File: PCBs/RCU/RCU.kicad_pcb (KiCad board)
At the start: 4 copper layers, 99 x 139 mm, 148 parts, among them J100 Conn_01x02, J200 USB_C_Receptacle_USB2.0, J201 Conn_01x05, J300 Right_Motor_Screw_Terminal, J301 Right_Encoder_Conn, J302 Left_Motor_Screw_Terminal, J303 Left_Encoder_Conn, J400 USB_C_Receptacle_USB2.0, Q400 2N7002NXAKR (NMOS), Q401 2N7002NXAKR (NMOS), Q402 BSS84AK,215 (PMOS), Q403 2N7002NXAKR (NMOS), SW201 SW_Push, SW400 SW_Push, SW401 SW_SPDT, U100 LM2576S-ADJ, U101 AP63203WU, U102 AZ1117-3.3, U200 STM32G0B1CBT6, U201 USBLC6-2SC6, U300 OPA320, U301 DRV8876, U302 OPA320, U303 DRV8876, U400 USBLC6-2SC6, U401 CH340C, U402 ESP32-MINI-1, U403 DG2788ADN-T1-GE4, U500 APDS-9306-065, U501 LSM6DS3, U502 SHT30-DIS, U600 ADC121C027CIMK/NOPB, U601 OPA320, U602 ADC121C027CIMK/NOPB, U603 OPA320, U700 SST26VF032BT-104I/SM, Y200 16MHz

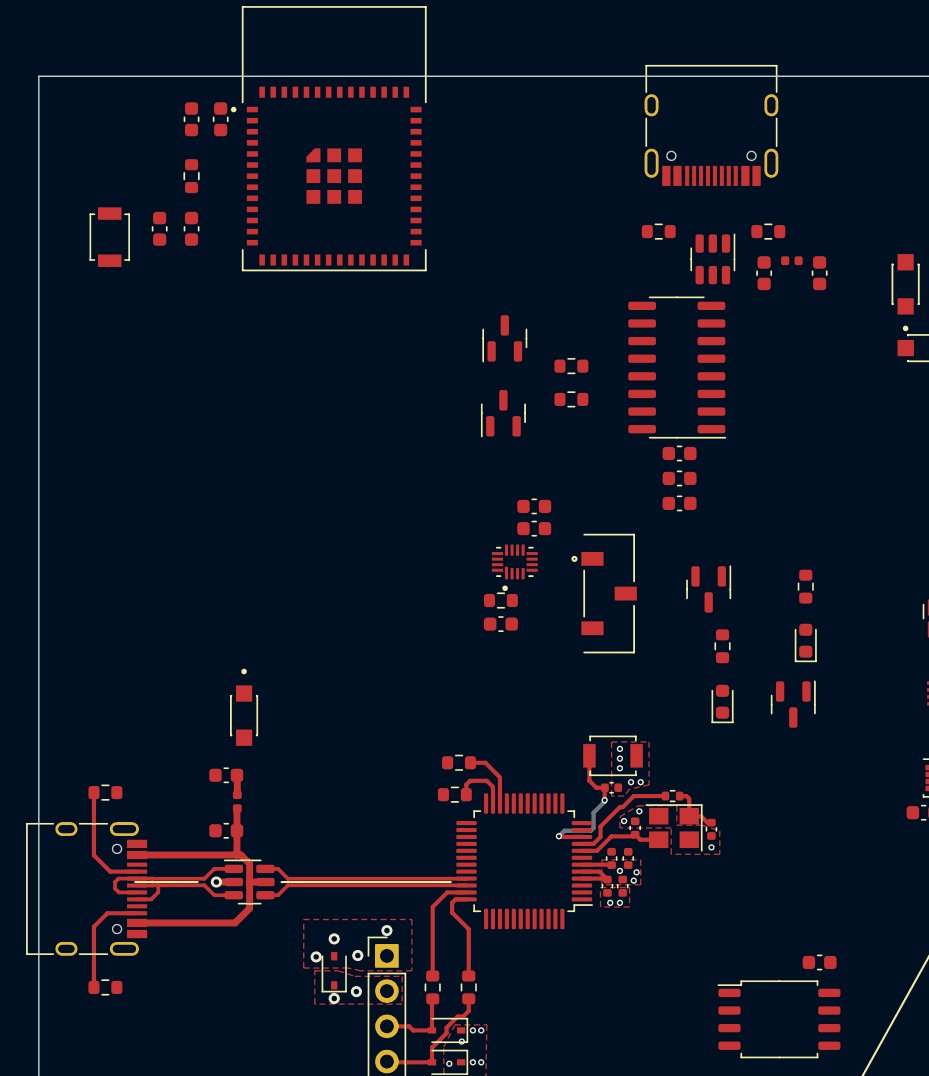
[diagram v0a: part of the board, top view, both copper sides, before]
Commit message: changed pad clearance of uart selector to 0.1mm
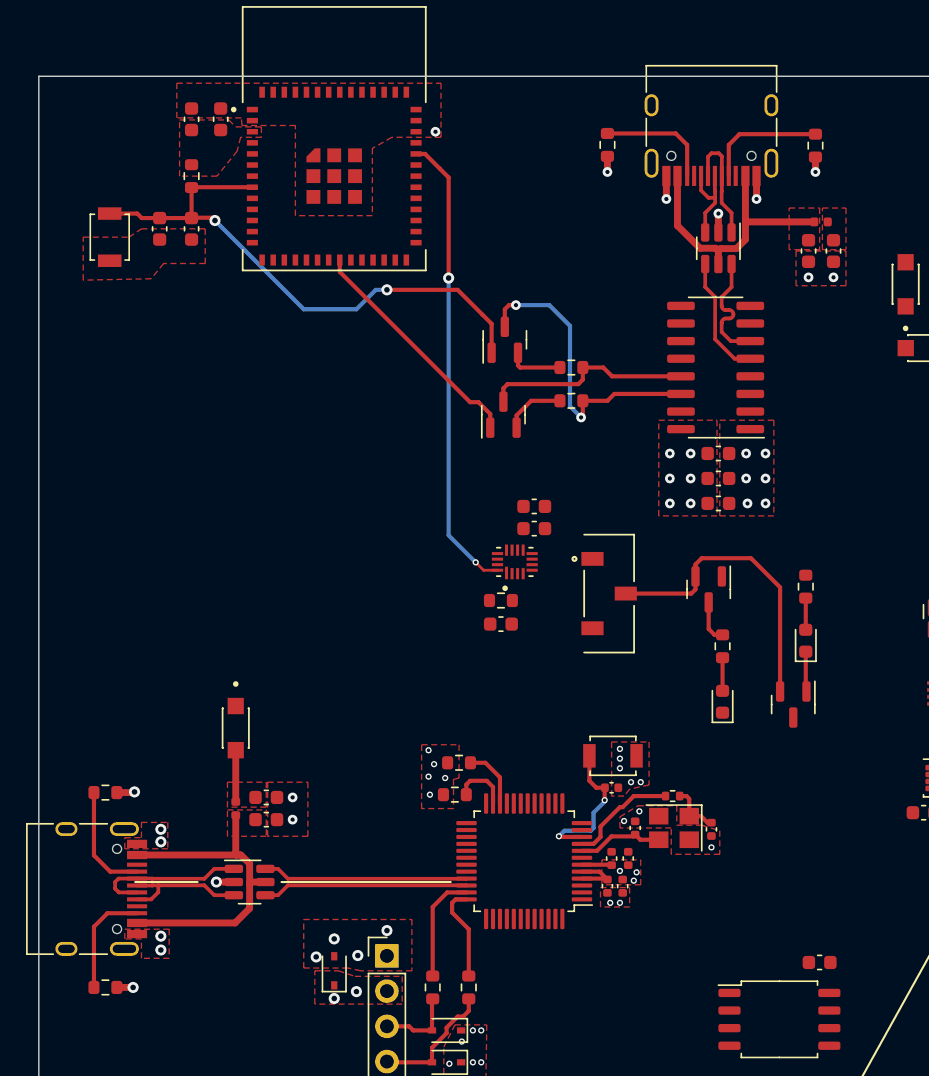
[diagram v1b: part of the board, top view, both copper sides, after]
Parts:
- moved R401 7.26 mm to (109.0, 25.9), turned to 90 degrees
- moved R400 7.07 mm to (124.0, 26.0), turned to -90 degrees
- moved C111 3.58 mm to (123.5, 33.6)
- moved L103 3.50 mm to (124.4, 31.5)
- moved C108 3.30 mm to (84.4, 73.0), turned to 0 degrees
- moved C107 3.00 mm to (84.4, 74.6), turned to 0 degrees
- moved C400 2.80 mm to (117.0, 51.8)
- moved C401 2.80 mm to (117.0, 50.0)
- moved C402 2.80 mm to (117.0, 48.2)
- moved U401 2.80 mm to (116.8, 42.0)
- moved C112 1.89 mm to (125.3, 33.6)
- moved D102 1.08 mm to (82.2, 68.0)
- moved U400 0.89 mm to (117.0, 33.4)
- moved L102 0.51 mm to (82.2, 73.8)
- moved Q400 0.10 mm to (101.5, 45.4)
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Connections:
- C111 pad 1: /[1] Power/VBUS2 -> VBUS2
- J200 pad S1: GND -> unconnected-(J200-PadS1)
- J400 pad A4: /[4] Bluetooth/VBUS2 -> VBUS2
- J400 pad A9: /[4] Bluetooth/VBUS2 -> VBUS2
- J400 pad B4: /[4] Bluetooth/VBUS2 -> VBUS2
- J400 pad B9: /[4] Bluetooth/VBUS2 -> VBUS2
- J400 pad S1: GND -> unconnected-(J400-PadS1)
- L103 pad 1: /[1] Power/VBUS2 -> VBUS2
- U400 pad 5: /[4] Bluetooth/VBUS2 -> VBUS2
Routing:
- net /[4] Bluetooth/BT_EN: track 0.00 -> 40.7 mm, vias 0 -> 2
- net UART_BT_TX: track 0.00 -> 33.4 mm, vias 0 -> 2
- net /[4] Bluetooth/RTS: track 0.00 -> 22.2 mm, vias 0 -> 2
- net /[4] Bluetooth/UART_SELECT: track 0.00 -> 21.6 mm
- net VBUS2: track 0.00 -> 20.1 mm
- net /[4] Bluetooth/IO0: track 0.00 -> 16.9 mm
- net /[4] Bluetooth/DTR: track 0.00 -> 15.2 mm
- net GND: track 1.26 -> 10.6 mm, vias 22 -> 44
- net /[4] Bluetooth/BT_D+: track 0.00 -> 8.84 mm
- net /[4] Bluetooth/CC1: track 0.00 -> 8.81 mm
- net /[4] Bluetooth/BT_D-: track 0.00 -> 8.67 mm
- net /[4] Bluetooth/BT_Raw_D-: track 0.00 -> 8.37 mm
- net /[4] Bluetooth/CC2: track 0.00 -> 8.33 mm
- net /[4] Bluetooth/BT_Raw_D+: track 0.00 -> 6.66 mm
- net /[4] Bluetooth/RTS_R: track 0.00 -> 4.45 mm
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- added copper zone on F.Cu, net +5C
- added copper zone on F.Cu, net +5F
- added copper zone on F.Cu, net VBUS1
- added copper zone on F.Cu, net VBUS2

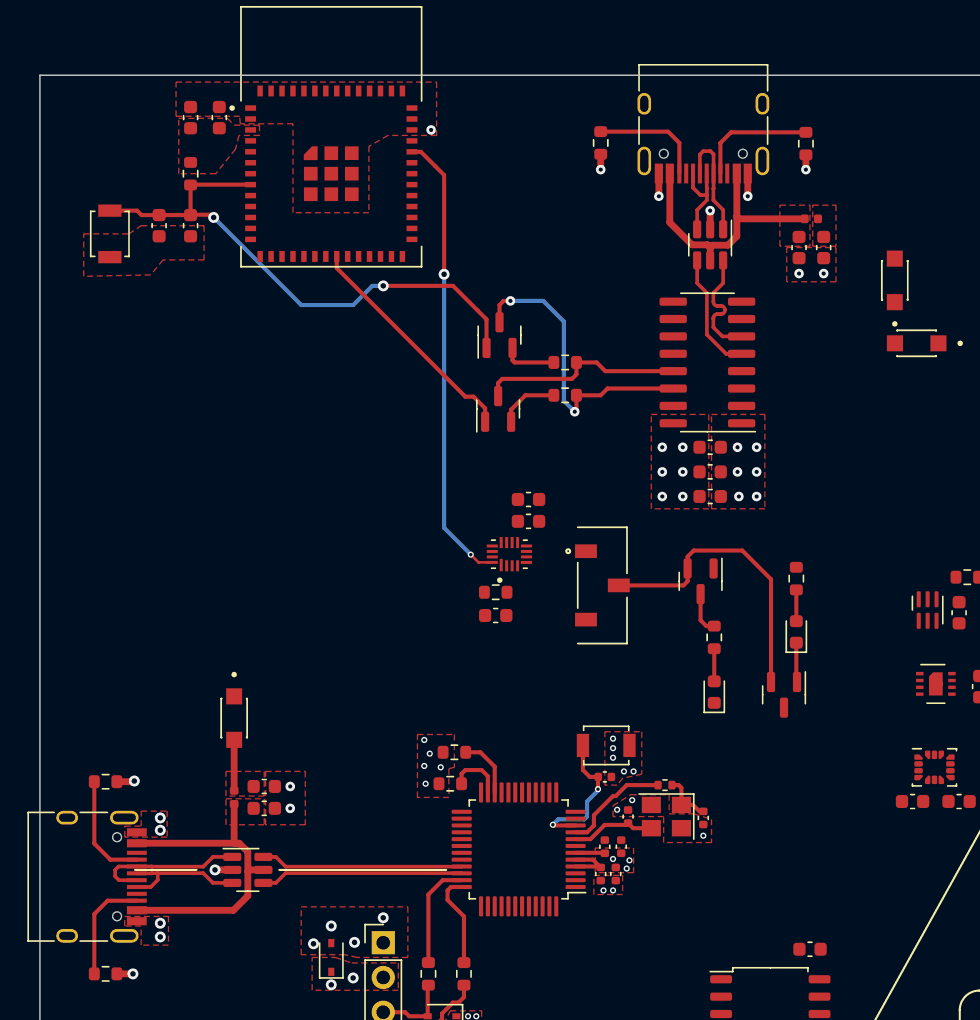
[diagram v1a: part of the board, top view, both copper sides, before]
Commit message: Completed tracing Bluetooth module
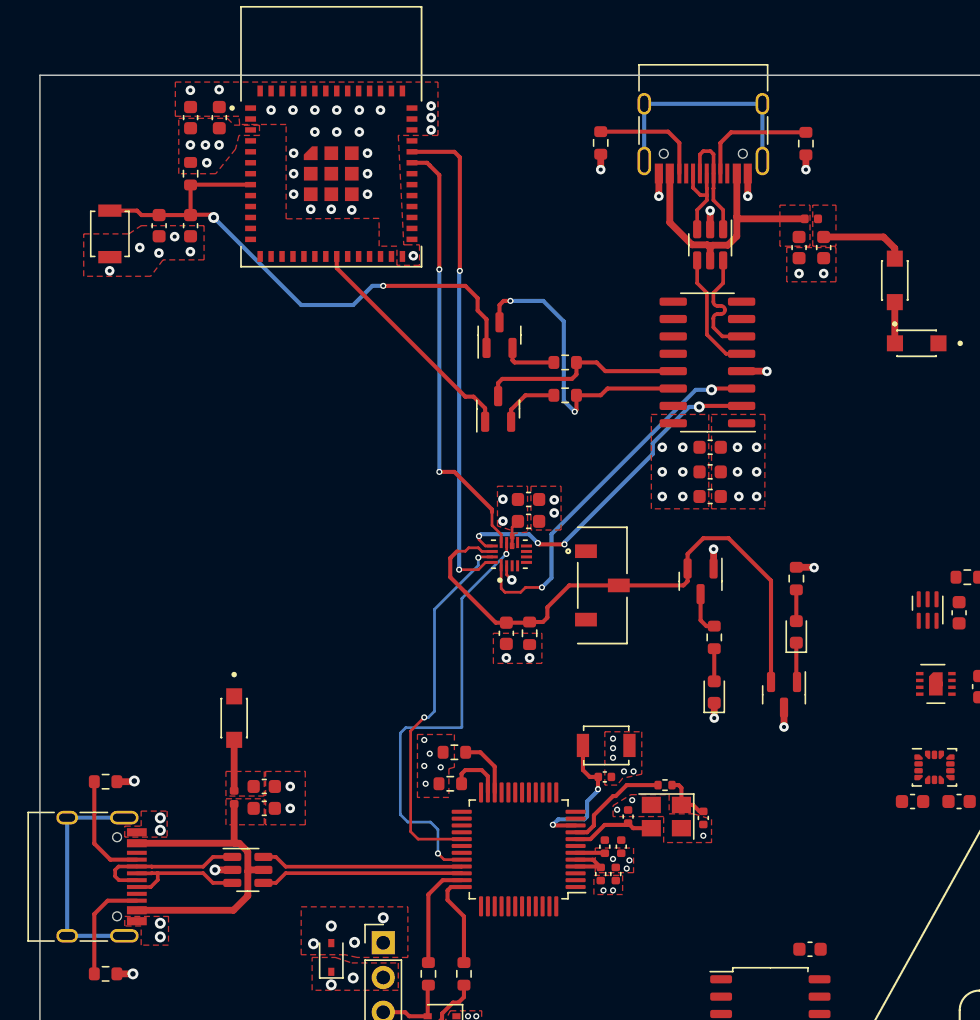
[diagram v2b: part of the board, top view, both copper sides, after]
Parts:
- moved R405 3.89 mm to (103.8, 61.8), turned to -90 degrees
- moved C409 1.52 mm to (102.1, 61.8), turned to -90 degrees
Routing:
- net UART_MCU_TX: track 0.00 -> 32.4 mm, vias 0 -> 2
- net UART_BT_RX: track 0.00 -> 31.8 mm, vias 0 -> 2
- net UART_PGR_RX: track 0.00 -> 27.4 mm, vias 0 -> 2
- net UART_MCU_RX: track 0.00 -> 27.3 mm, vias 0 -> 2
- net UART_PGR_TX: track 0.00 -> 25.7 mm, vias 0 -> 4
- net /[4] Bluetooth/UART_SELECT: track 21.6 -> 42.6 mm
- net unconnected-(J200-PadS1): track 0.00 -> 17.0 mm
- net unconnected-(J400-PadS1): track 0.00 -> 17.0 mm
- net +3V3: track 6.09 -> 12.4 mm, vias 18 -> 27
- net +5F: track 0.00 -> 6.30 mm
- net GND: track 10.6 -> 14.3 mm, vias 44 -> 79
- net UART_BT_TX: track 33.4 -> 36.5 mm
- net Net-(D103-Pad1): track 0.00 -> 3.01 mm
- net /[4] Bluetooth/BT_EN: track 40.7 -> 41.2 mm

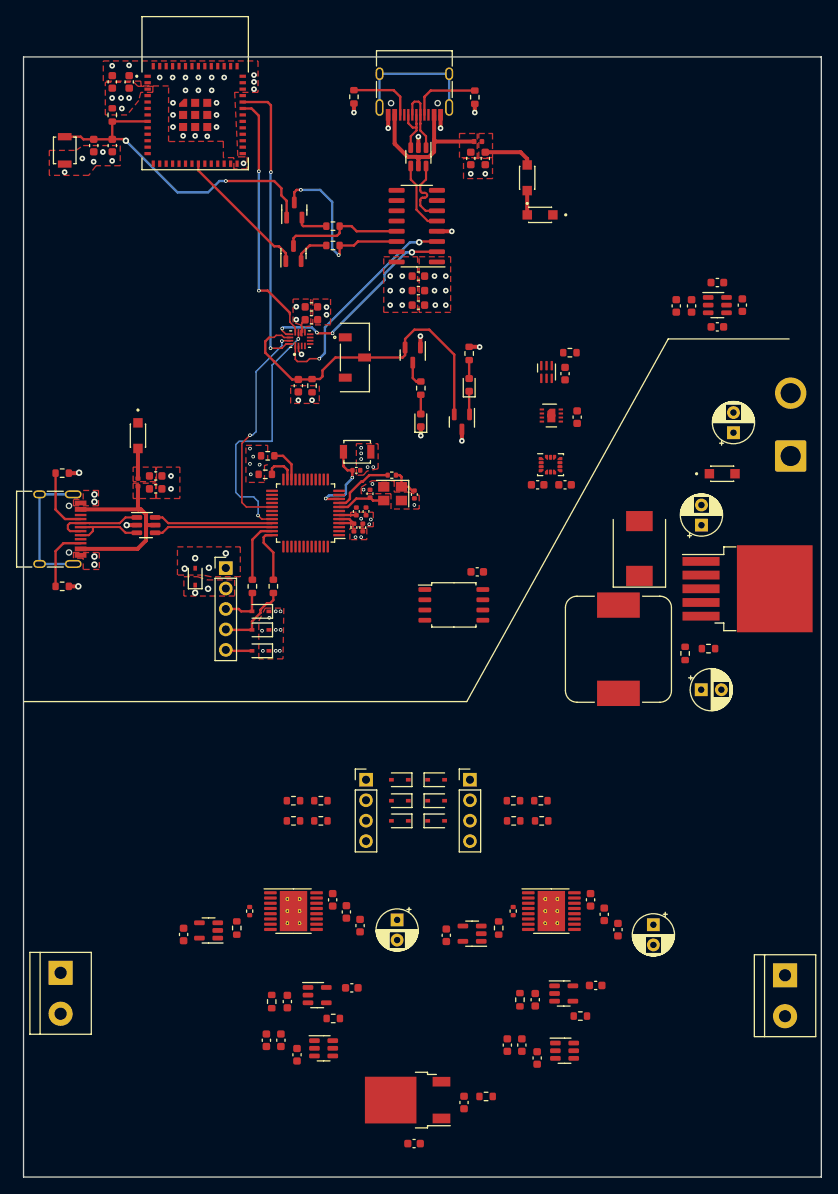
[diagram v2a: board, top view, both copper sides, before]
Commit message: Finished routing 3.3V regulator
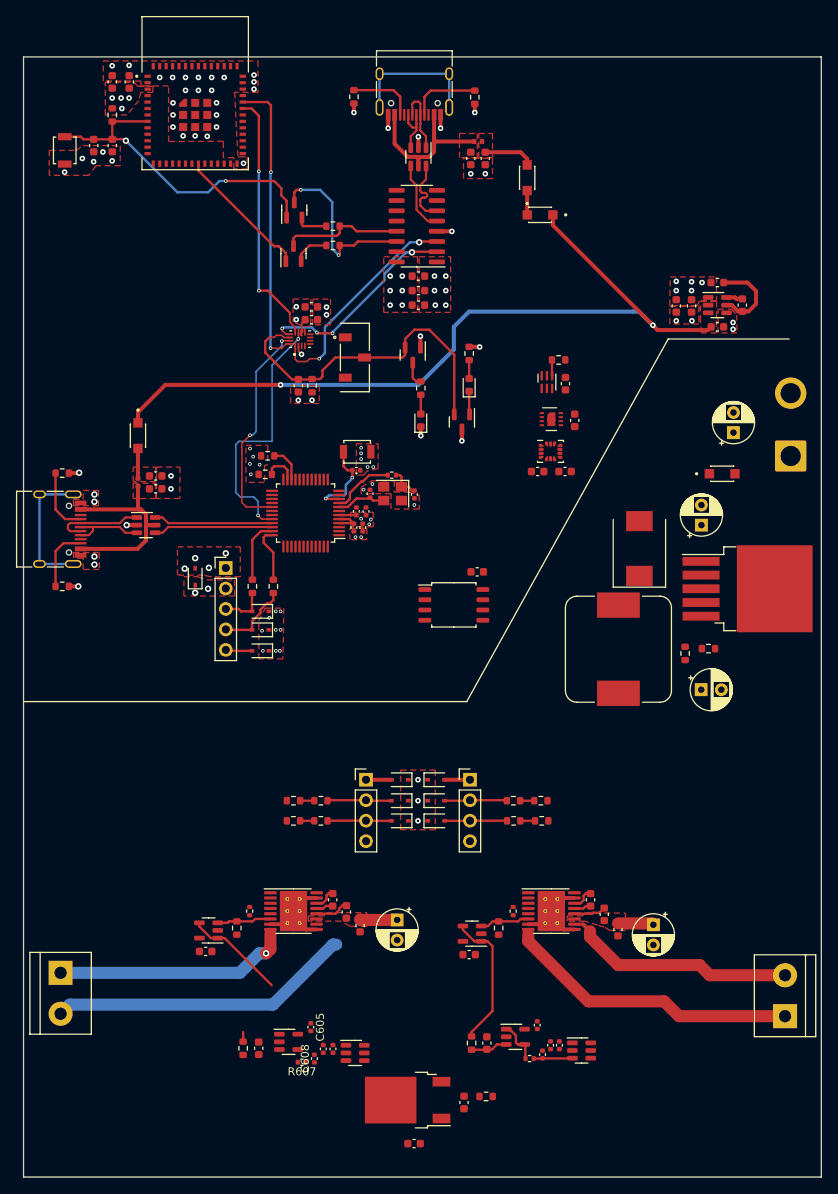
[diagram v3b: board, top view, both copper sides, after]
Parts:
- C600, C601, C602, C603, C605, C606, C607, C608: footprint Capacitor_SMD:C_0603_1608Metric -> Capacitor_SMD:C_0402_1005Metric
- R600, R607: footprint Resistor_SMD:R_0603_1608Metric -> Resistor_SMD:R_0402_1005Metric
- moved C601 35.3 mm to (133.4, 143.7)
- moved C602 34.6 mm to (134.5, 143.7)
- moved C607 23.4 mm to (106.4, 144.1)
- moved C606 22.8 mm to (105.2, 144.1)
- moved C600 8.76 mm to (131.8, 141.2), turned to -90 degrees
- moved R600 8.22 mm to (130.8, 145.3)
- moved C604 8.06 mm to (125.5, 143.4)
- moved R601 8.06 mm to (123.6, 143.4)
- moved U601 8.06 mm to (129.0, 142.6)
- moved C605 7.05 mm to (103.7, 141.4), turned to -90 degrees
- moved C609 6.80 mm to (97.2, 144.0)
- moved R603 6.80 mm to (95.2, 144.0)
- moved U603 6.80 mm to (100.9, 143.2)
- moved R607 6.67 mm to (102.5, 145.8)
- moved J300 5.08 mm to (162.5, 140.0), turned to 90 degrees
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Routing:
- net VCOM: track 0.00 -> 99.2 mm, vias 0 -> 2
- net /[3] Motor_Control/Left_Out2: track 0.00 -> 37.8 mm
- net /[3] Motor_Control/Right_Out1: track 0.00 -> 36.6 mm
- net /[3] Motor_Control/Right_Out2: track 0.00 -> 29.2 mm
- net /[3] Motor_Control/Left_Out1: track 0.00 -> 29.1 mm, vias 0 -> 1
- net Buffered_Right_Sensed_Motor_Current: track 0.00 -> 17.3 mm
- net +6V: track 0.00 -> 15.4 mm
- net Buffered_Left_Sensed_Motor_Current: track 0.00 -> 13.7 mm
- net GND: track 14.3 -> 27.9 mm, vias 79 -> 86
- net /[1] Power/SWO_100: track 0.00 -> 10.4 mm
- net /[3] Motor_Control/6V_LeftA_Output: track 0.00 -> 7.97 mm
- net /[3] Motor_Control/6V_LeftB_Output: track 0.00 -> 7.94 mm
- net /[3] Motor_Control/6V_RightA_Output: track 0.00 -> 7.77 mm
- net /[3] Motor_Control/6V_RightB_Output: track 0.00 -> 7.77 mm
- net /[3] Motor_Control/Left_Sensed_Motor_Current: track 0.00 -> 6.73 mm
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- added copper zone on F.Cu, net +6V
- added copper zone on F.Cu, net VCOM

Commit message: laid and routed Current feedback
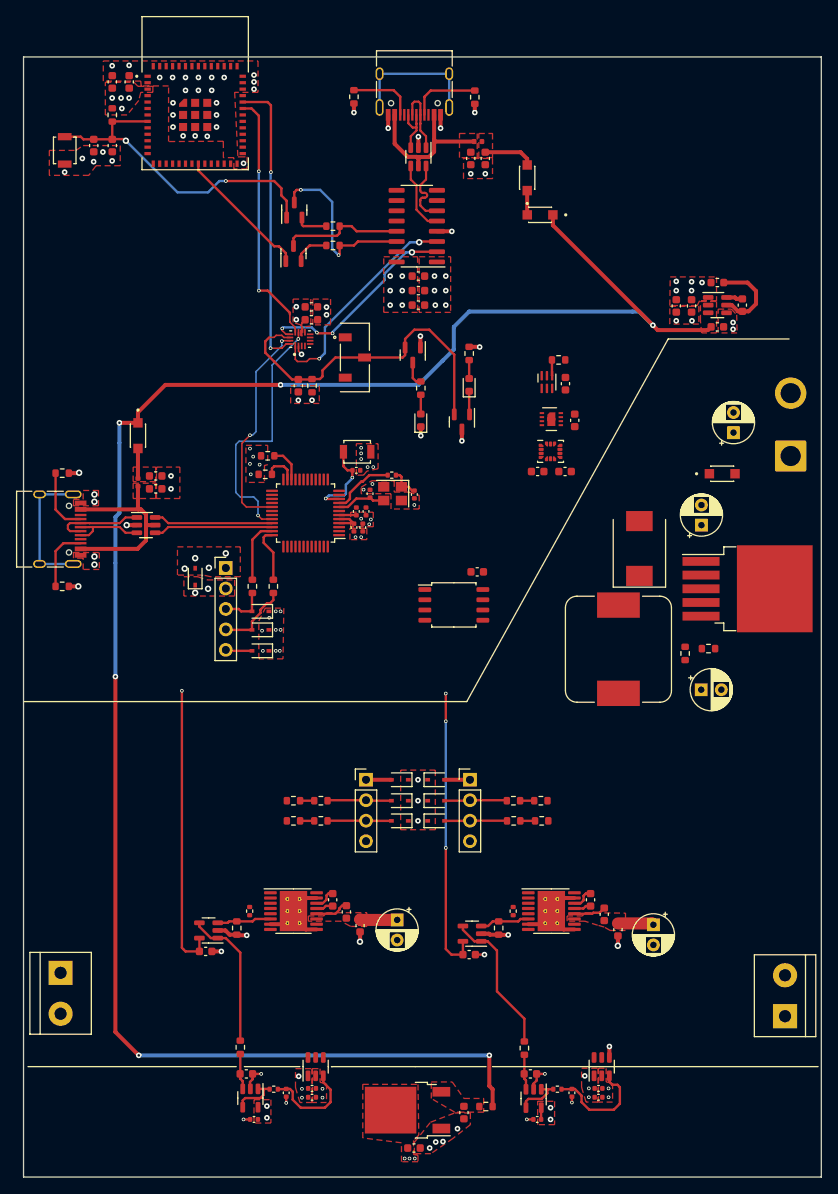
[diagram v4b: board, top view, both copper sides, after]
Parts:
- moved C605 13.4 mm to (96.6, 152.8), turned to 0 degrees
- moved C600 11.7 mm to (131.8, 152.8), turned to 0 degrees
- moved C601 8.78 mm to (139.3, 150.1), turned to 0 degrees
- moved U603 8.43 mm to (96.2, 150.2), turned to -90 degrees
- moved U601 7.98 mm to (131.3, 150.2), turned to -90 degrees
- moved C602 7.22 mm to (139.3, 149.0), turned to 0 degrees
- moved C604 6.62 mm to (130.9, 147.2), turned to 180 degrees
- moved R601 6.58 mm to (130.2, 144.0)
- moved C606 6.16 mm to (103.8, 150.1), turned to 0 degrees
- moved C603 5.99 mm to (136.1, 149.6), turned to -90 degrees
- moved C607 5.55 mm to (103.8, 149.0), turned to 0 degrees
- moved C608 5.51 mm to (100.6, 149.6), turned to -90 degrees
- moved U602 5.19 mm to (104.2, 146.3), turned to 90 degrees
- moved R600 5.13 mm to (134.2, 149.1)
- moved R607 4.84 mm to (99.0, 149.1)
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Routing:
- net VCOM: track 99.2 -> 231.4 mm, vias 2 -> 6
- net +3V3: track 12.4 -> 84.1 mm, vias 32 -> 36
- net /[3] Motor_Control/Left_Out2: track 37.8 -> 0.00 mm
- net /[3] Motor_Control/Right_Out1: track 36.6 -> 0.00 mm
- net /[3] Motor_Control/Right_Out2: track 29.2 -> 0.00 mm
- net /[3] Motor_Control/Left_Out1: track 29.1 -> 0.00 mm, vias 1 -> 0
- net GND: track 27.9 -> 50.5 mm, vias 86 -> 107
- net /[6] ADCs/ADC_RIGHT_IN: track 0.00 -> 12.0 mm
- net /[6] ADCs/ADC_LEFT_IN: track 4.82 -> 13.5 mm
- net /[6] ADCs/LEFT_AMP_OUT: track 0.00 -> 5.88 mm
- net Net-(C609-Pad2): track 0.00 -> 4.48 mm
- net Buffered_Left_Sensed_Motor_Current: track 13.7 -> 17.8 mm
- net +3.3VA: track 0.00 -> 1.47 mm, vias 0 -> 13
- net Buffered_Right_Sensed_Motor_Current: track 17.3 -> 18.4 mm
- added copper zone on F.Cu, net +3.3VA
- added copper zone on In2.Cu, net +3.3VA
- added copper zone on F.Cu, net /[1] Power/BATT_FILT
